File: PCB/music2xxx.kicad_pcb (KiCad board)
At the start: 2 copper layers, 100 x 150 mm, 50 parts, among them IC1 74HCT74, IC10 74HCT08, IC2 74HCT75, IC3 74HCT32, IC4 74HCT138, IC5 74HCT08, IC6 MC6850, IC7 MC6850, IC8 MC6850, IC9 6N137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

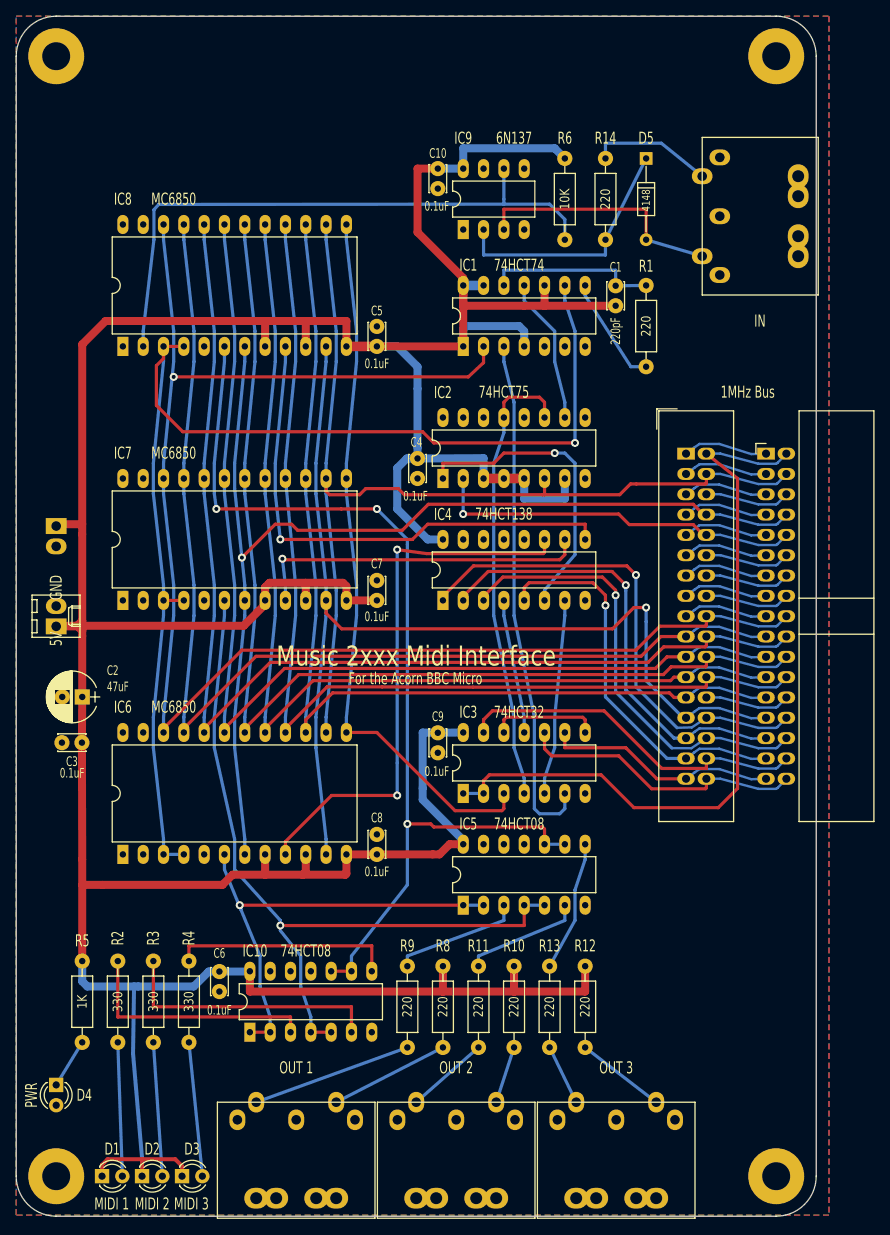
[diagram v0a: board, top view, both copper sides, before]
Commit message: Add 7805 regulator
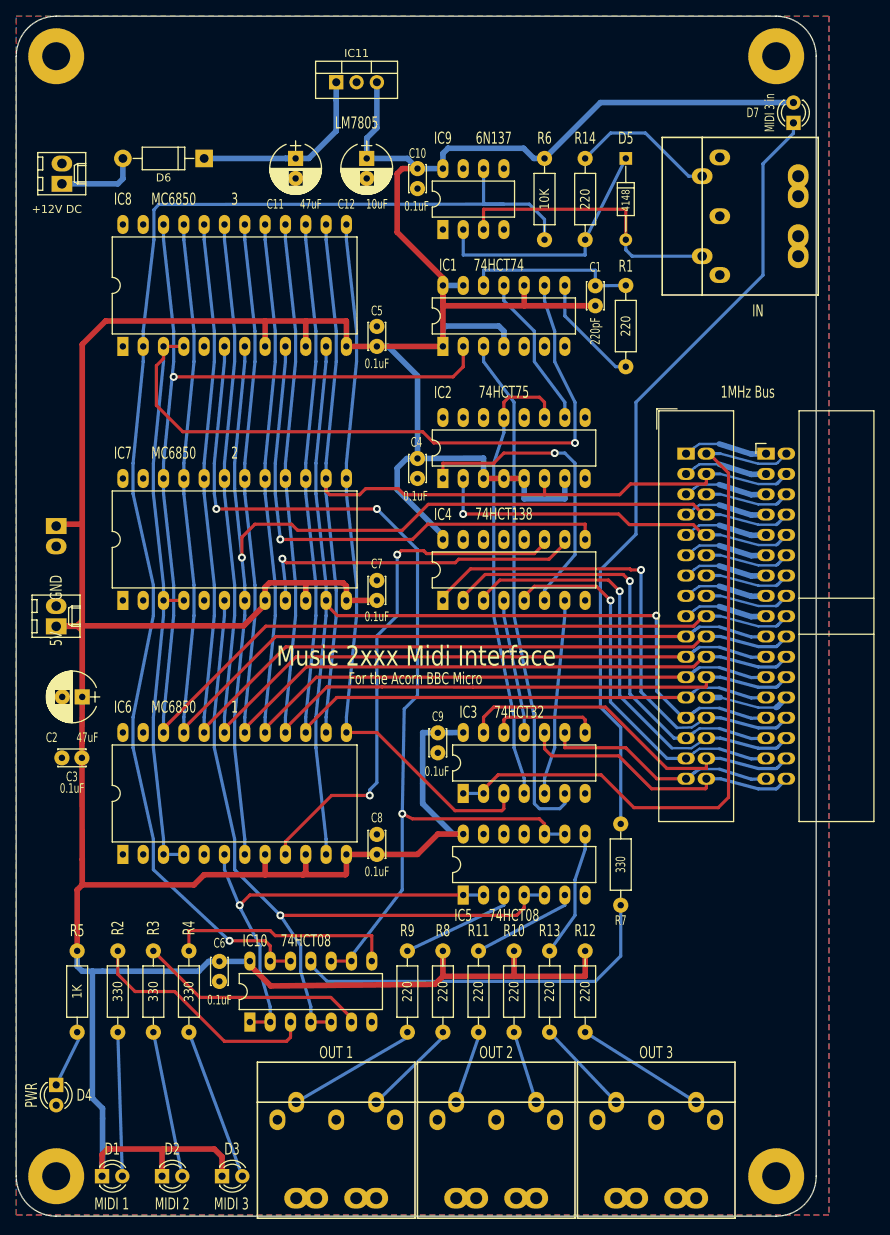
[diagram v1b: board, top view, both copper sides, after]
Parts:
- added C11: 47uF, musix5xxx-custom:CP_Radial_D6.3mm_P2.50mm, F.Cu at (34.9, 17.8)
- added C2: 47uF, musix5xxx-custom:CP_Radial_D6.3mm_P2.50mm, F.Cu at (8.26, 85.1)
- added D6: 1N4001, Diodes_THT:D_DO-41_SOD81_P10.16mm_Horizontal, F.Cu at (23.5, 17.8)
- added D7: MIDI 3 in, musix5xxx-custom:LED_D3.0mm, F.Cu at (97.2, 12.1)
- added IC11: LM7805_TO220, TO_SOT_Packages_THT:TO-220-3_Vertical, F.Cu at (40.0, 8.26)
- added J9: +12V DC, Connectors_Molex:Molex_KK-6410-02_02x2.54mm_Straight, F.Cu at (5.71, 21.0)
- added R7: 330, musix5xxx-custom:R_Axial_DIN0207_L6.3mm_D2.5mm_P10.16mm_Horizontal, F.Cu at (75.6, 111.1)
- C12: renamed from C2; value 47uF -> 10uF
- moved C12 76.1 mm to (43.8, 17.8), turned to 270 degrees
- moved D3 5.00 mm to (27.0, 145.0)
- moved J5 5.00 mm to (40.0, 143.0)
- moved J6 5.00 mm to (60.0, 143.0)
- moved J7 5.00 mm to (80.0, 143.0)
- moved C1 2.54 mm to (72.4, 36.2)
- moved C10 2.54 mm to (50.2, 19.1)
- moved IC1 2.54 mm to (53.3, 41.3)
- moved IC9 2.54 mm to (53.3, 26.7)
- moved D5 2.54 mm to (76.2, 17.8)
- moved R1 2.54 mm to (76.2, 43.8)
- moved R14 2.54 mm to (71.1, 27.9)
- moved R6 2.54 mm to (66.0, 27.9)
- moved D2 2.50 mm to (19.5, 145.0)
- moved R10 1.91 mm to (62.2, 116.8)
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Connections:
- IC10 pad 12: GND -> RX3
- IC10 pad 13: GND -> RX3
- IC8 pad 2: Net-(IC8-Pad2) -> RX3
- IC9 pad 6: Net-(IC8-Pad2) -> RX3
- R6 pad 1: Net-(IC8-Pad2) -> RX3
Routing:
- net RX3: track 0.00 -> 165.7 mm, vias 0 -> 1
- net Net-(D7-Pad1): track 0.00 -> 98.7 mm
- net Net-(IC8-Pad2): track 76.6 -> 0.00 mm
- net +5V: track 531.2 -> 586.5 mm
- net Net-(IC10-Pad11): track 0.00 -> 48.2 mm
- net Net-(C11-Pad1): track 0.00 -> 26.4 mm
- net Net-(D6-Pad2): track 0.00 -> 10.4 mm
- net Net-(J7-Pad4): track 11.2 -> 16.4 mm
- net Net-(IC10-Pad6): track 33.7 -> 28.7 mm
- net Net-(J7-Pad5): track 7.61 -> 12.1 mm
- net Net-(J5-Pad5): track 20.1 -> 16.1 mm
- net Net-(D5-Pad2): track 31.4 -> 35.3 mm
- net Net-(J5-Pad4): track 15.0 -> 11.6 mm
- net CS2-1: track 69.3 -> 66.3 mm
- net /d0: track 190.8 -> 187.9 mm
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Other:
- net class PWR: trace_width 1 -> 0.7
- board text added: "1"
- board text added: "2"
- board text added: "3"
- board text added: "Based on Hybrid M2000 Midi Interface This PCB and mods by J Lane September 2019"
- board text added: "LM7805"
- board text removed: "Based on Hybrid M2000 Midi Interface This PCB and mods by J Lane May 2019"
